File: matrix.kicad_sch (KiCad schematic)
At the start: 94 parts, among them SW1 SW_PUSH, SW10 SW_PUSH, SW11 SW_PUSH, SW12 SW_PUSH, SW13 SW_PUSH, SW14 SW_PUSH, SW15 SW_PUSH, SW16 SW_PUSH, SW17 SW_PUSH, SW18 SW_PUSH, SW19 SW_PUSH, SW2 SW_PUSH, SW20 SW_PUSH, SW21 SW_PUSH, SW22 SW_PUSH, SW23 SW_PUSH, SW24 SW_PUSH, SW25 SW_PUSH, SW26 SW_PUSH, SW27 SW_PUSH, SW28 SW_PUSH, SW29 SW_PUSH, SW3 SW_PUSH, SW30 SW_PUSH, SW31 SW_PUSH, SW32 SW_PUSH, SW33 SW_PUSH, SW34 SW_PUSH, SW35 SW_PUSH, SW36 SW_PUSH, SW37 SW_PUSH, SW38 SW_PUSH, SW39 SW_PUSH, SW4 SW_PUSH, SW40 SW_PUSH, SW41 SW_PUSH, SW42 SW_PUSH, SW43 SW_PUSH, SW44 SW_PUSH, SW45 SW_PUSH, SW46 SW_PUSH, SW47 SW_PUSH, SW5 SW_PUSH, SW6 SW_PUSH, SW7 SW_PUSH, SW8 SW_PUSH, SW9 SW_PUSH

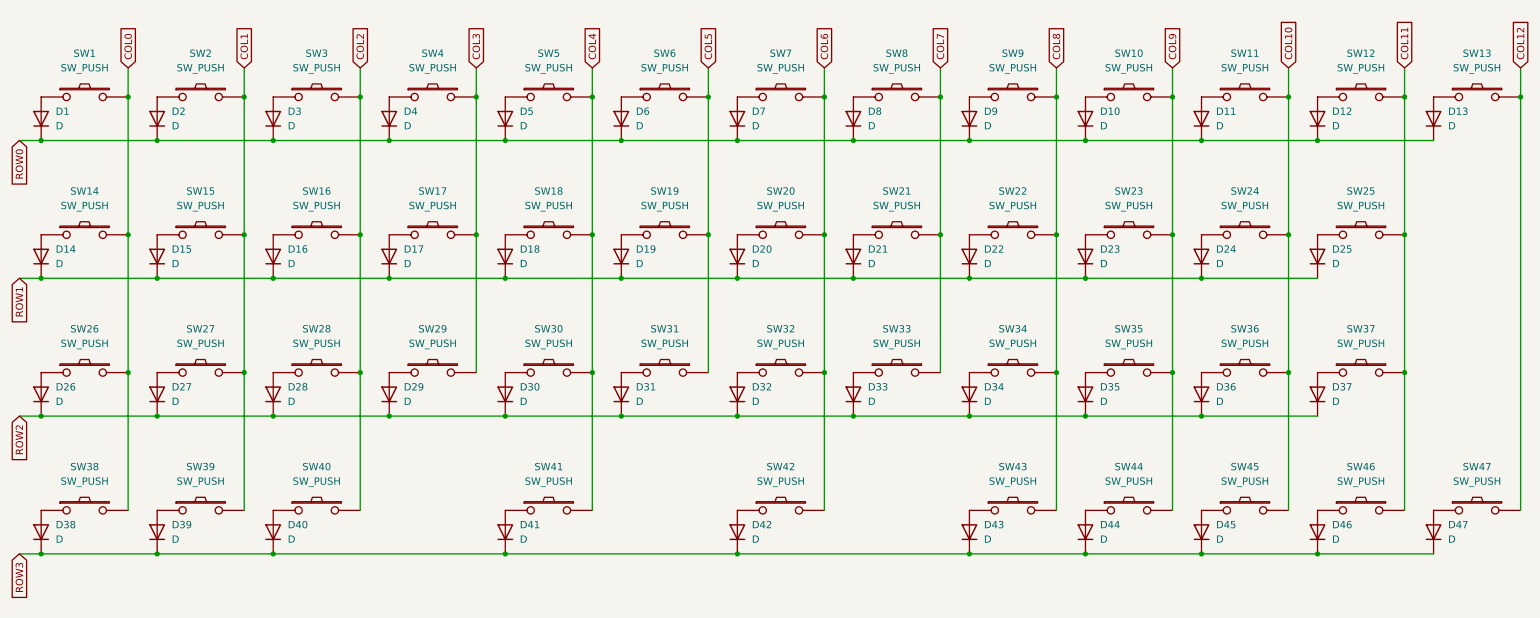
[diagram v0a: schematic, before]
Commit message: 1/21
changed layout to teeth version, started routing rows and columns
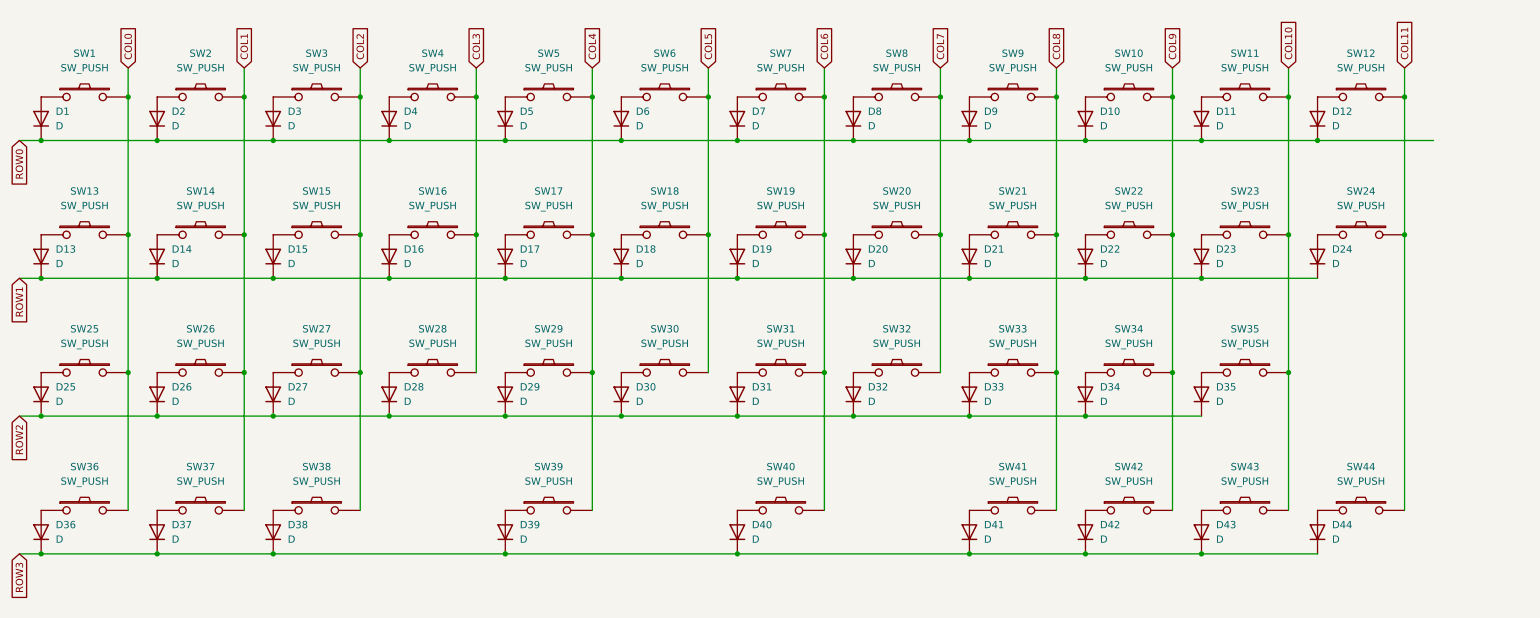
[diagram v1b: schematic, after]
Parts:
- removed D13, D37, D47: D, Diode_SMD:D_SOD-123, symbol Device:D
- removed SW13, SW37, SW47: SW_PUSH, emptystring:MXOnly-1U-Hotswap, symbol kbd:SW_PUSH
- renumbered D14 to D13, D15 to D14, D16 to D15, D17 to D16, D18 to D17, D19 to D18, D20 to D19, D21 to D20, D22 to D21, D23 to D22, D24 to D23, D25 to D24, D26 to D25, D27 to D26, D28 to D27, D29 to D28, D30 to D29, D31 to D30, D32 to D31, D33 to D32, D34 to D33, D35 to D34, D36 to D35, D38 to D36, D39 to D37, D40 to D38, D41 to D39, D42 to D40, D43 to D41, D44 to D42, D45 to D43, D46 to D44, SW14 to SW13, SW15 to SW14, SW16 to SW15, SW17 to SW16, SW18 to SW17, SW19 to SW18, SW20 to SW19, SW21 to SW20, SW22 to SW21, SW23 to SW22, SW24 to SW23, SW25 to SW24, SW26 to SW25, SW27 to SW26, SW28 to SW27, SW29 to SW28, SW30 to SW29, SW31 to SW30, SW32 to SW31, SW33 to SW32, SW34 to SW33, SW35 to SW34, SW36 to SW35, SW38 to SW36, SW39 to SW37, SW40 to SW38, SW41 to SW39, SW42 to SW40, SW43 to SW41, SW44 to SW42, SW45 to SW43, SW46 to SW44
